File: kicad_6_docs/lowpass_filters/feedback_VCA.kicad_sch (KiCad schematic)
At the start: 15 parts, among them U2 TL072, U3 SSI2164, U4 TL072

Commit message: Initial filter board layout
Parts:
- R77: value 100k -> 330k
- R79: value 100k -> 680k
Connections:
- net -5VA renamed -15V
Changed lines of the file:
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@@
     (in_bom yes) (on_board yes)
     (property "Reference" "R79" (id 0) (at 100.33 148.4122 90))
-    (property "Value" "100k" (id 1) (at 100.33 150.7236 90))
+    (property "Value" "680k" (id 1) (at 100.33 150.7236 90))
     (property "Footprint" "Resistor_SMD:R_0805_2012Metric" (id 2) (at 100.33 151.892 90)
       (effects (font (size 1.27 1.27)) hide)
@@
     (pin "1")
   )
-  (symbol (lib_id "power:-5VA") (at 151.13 125.73 0) (mirror x) (unit 1)
-    (in_bom yes) (on_board yes)
-    (property "Reference" "#PWR0143" (id 0) (at 151.13 128.27 0)
-      (effects (font (size 1.27 1.27)) hide)
-    )
-    (property "Value" "-5VA" (id 1) (at 151.511 130.1242 0))
+  (symbol (lib_id "power:-15V") (at 151.13 125.73 180) (unit 1)
+    (in_bom yes) (on_board yes) (fields_autoplaced)
+    (property "Reference" "#PWR?" (id 0) (at 151.13 128.27 0)
+      (effects (font (size 1.27 1.27)) hide)
+    )
+    (property "Value" "-15V" (id 1) (at 151.13 130.81 0))
     (property "Footprint" "" (id 2) (at 151.13 125.73 0)
       (effects (font (size 1.27 1.27)) hide)
@@
     (in_bom yes) (on_board yes)
     (property "Reference" "R77" (id 0) (at 144.78 117.9322 90))
-    (property "Value" "100k" (id 1) (at 144.78 120.2436 90))
+    (property "Value" "330k" (id 1) (at 144.78 120.2436 90))
     (property "Footprint" "Resistor_SMD:R_0805_2012Metric" (id 2) (at 144.78 121.412 90)
       (effects (font (size 1.27 1.27)) hide)

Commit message: Filter board rev 0 and outputs
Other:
- title: (none) -> M.S.M. Stereo Lowpass Filter Pedal
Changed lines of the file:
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@@
 (kicad_sch (version 20211123) (generator eeschema)
   (paper "A4")
+  (title_block
+    (title "M.S.M. Stereo Lowpass Filter Pedal")
+    (date "2022-05-24")
+    (rev "0")
+    (comment 2 "creativecommons.org/licenses/by/4.0")
+    (comment 3 "License: CC by 4.0")
+    (comment 4 "Author: Jordan Aceto")
+  )
   (junction (at 180.34 68.58) (diameter 0) (color 0 0 0 0)
   )
@@
   (symbol (lib_id "power:-15V") (at 151.13 125.73 180) (unit 1)
     (in_bom yes) (on_board yes) (fields_autoplaced)
-    (property "Reference" "#PWR?" (id 0) (at 151.13 128.27 0)
-      (effects (font (size 1.27 1.27)) hide)
-    )
+    (property "Reference" "#PWR026" (id 0) (at 151.13 128.27 0)
+      (effects (font (size 1.27 1.27)) hide)
+    )

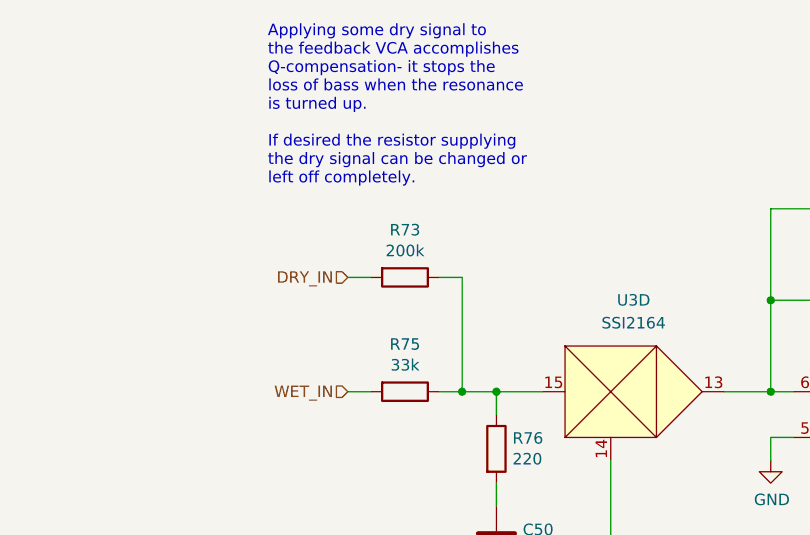
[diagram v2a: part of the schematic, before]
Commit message: Tweak some filter board values
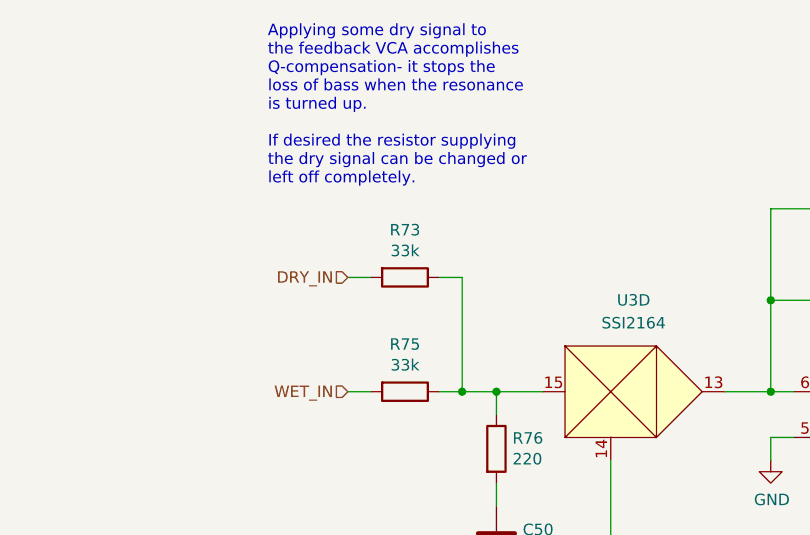
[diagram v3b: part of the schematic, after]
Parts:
- R73: value 200k -> 33k
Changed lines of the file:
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@@
   (title_block
     (title "M.S.M. Stereo Lowpass Filter Pedal")
-    (date "2022-05-24")
+    (date "2022-06-16")
     (rev "0")
     (comment 2 "creativecommons.org/licenses/by/4.0")
@@
     (in_bom yes) (on_board yes)
     (property "Reference" "R73" (id 0) (at 139.7 50.6222 90))
-    (property "Value" "200k" (id 1) (at 139.7 52.9336 90))
+    (property "Value" "33k" (id 1) (at 139.7 52.9336 90))
     (property "Footprint" "Resistor_SMD:R_0805_2012Metric" (id 2) (at 139.7 54.102 90)
       (effects (font (size 1.27 1.27)) hide)
